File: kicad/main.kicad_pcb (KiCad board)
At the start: 2 copper layers, 200 x 100 mm, 50 parts, among them J1 Barrel_Jack, J2 UART, P1 Mini-DIN_6pins_ver3, SW1 Reset, SW2 SW_Push_DPDT, U1 KM1810VM88, U10 L7805, U11 15 MHz, U12 8255, U13 uSD adapter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

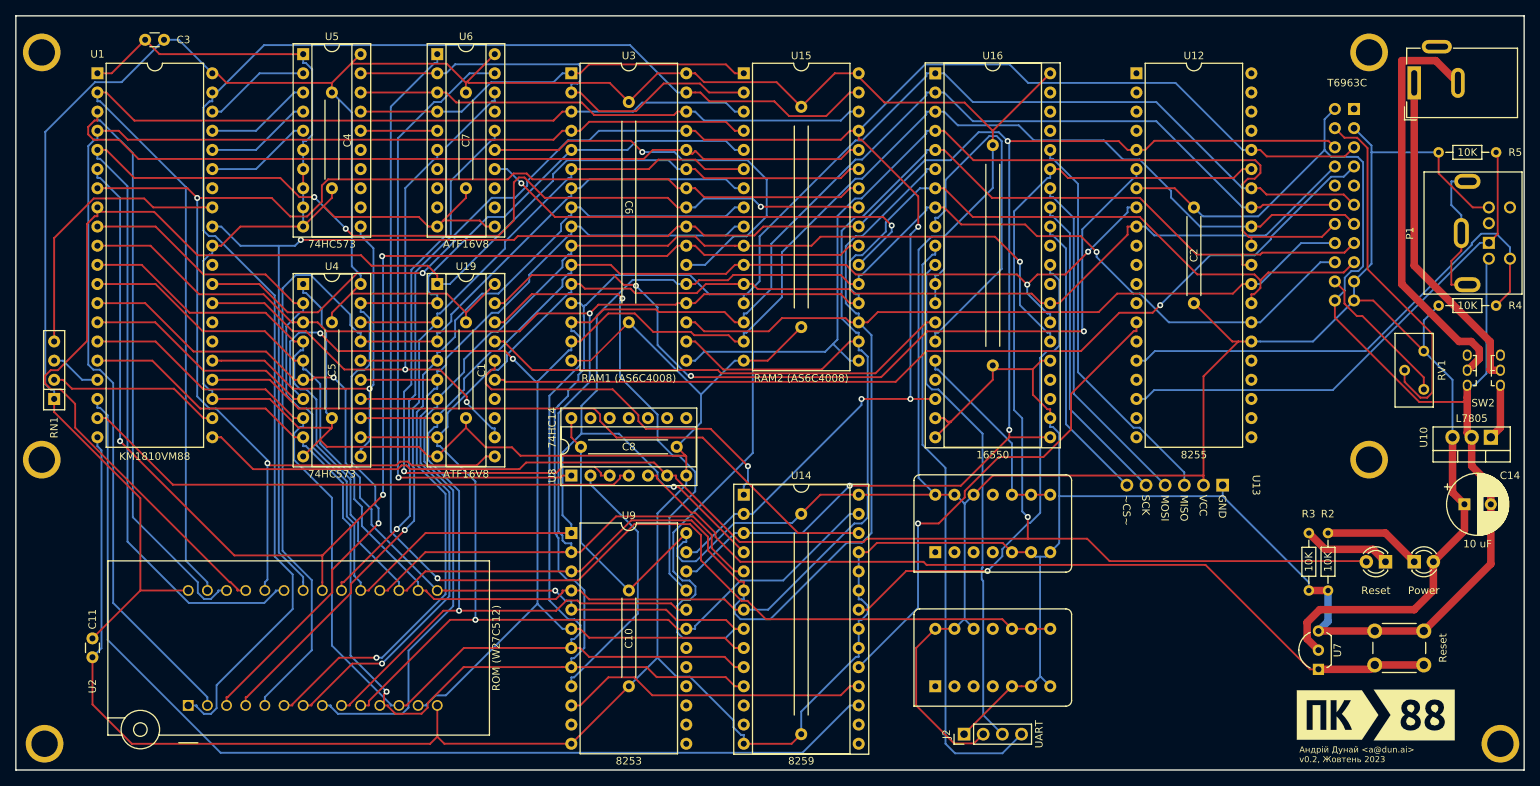
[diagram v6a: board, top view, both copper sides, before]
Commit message: New PCB (add MCB line)
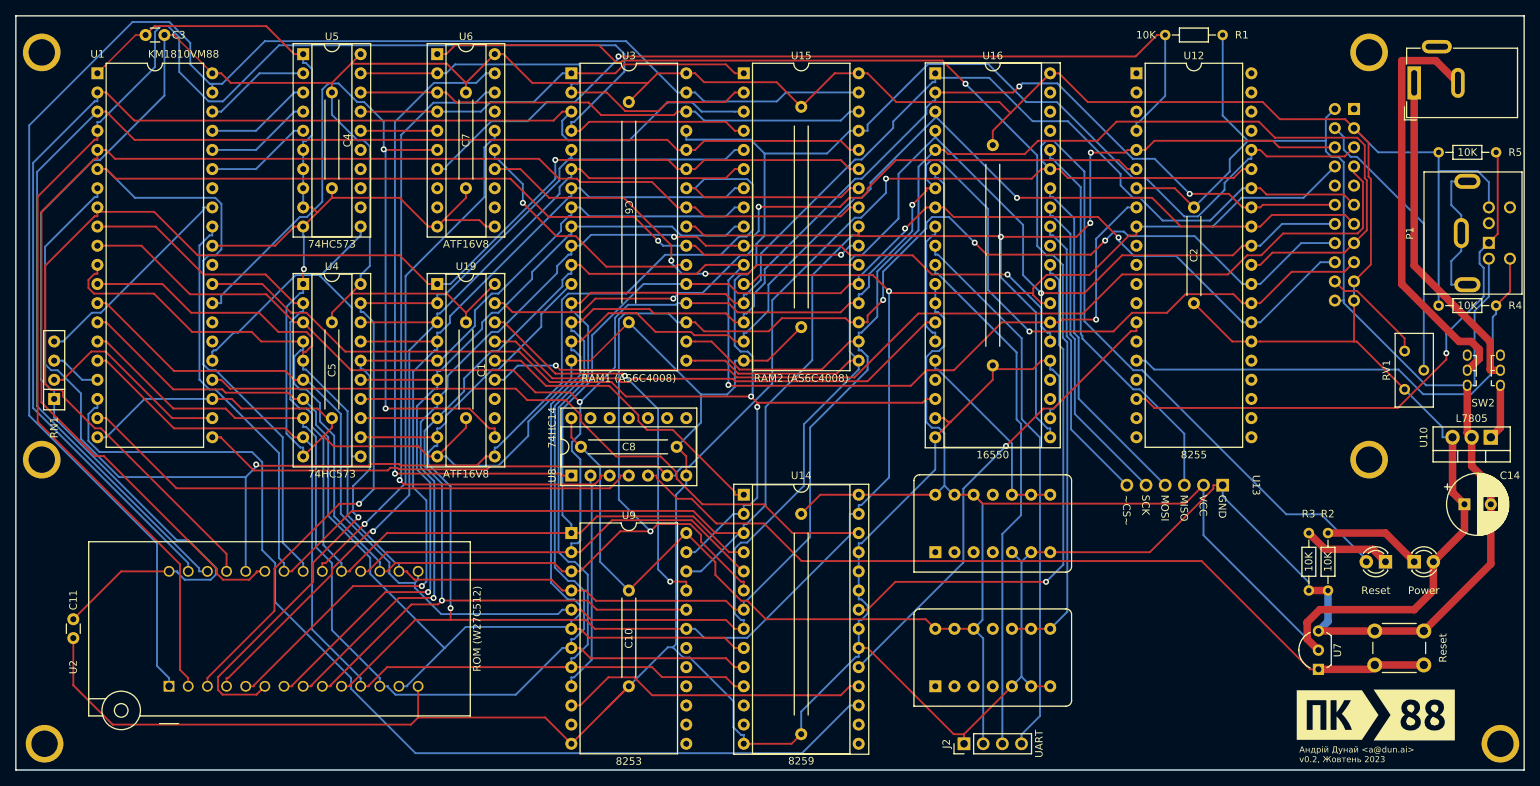
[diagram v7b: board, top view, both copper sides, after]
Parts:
- added R1: 10K, Resistor_THT:R_Axial_DIN0204_L3.6mm_D1.6mm_P7.62mm_Horizontal, F.Cu at (180.3, 20.3)
- moved RV1 5.68 mm to (204.5, 62.2), turned to 90 degrees
- moved C11 3.59 mm to (27.9, 97.8)
- moved U2 3.59 mm to (40.6, 106.7)
- moved J2 1.27 mm to (146.1, 114.3)
- moved C3 0.64 mm to (40.0, 20.3)
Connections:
- U12 pad 4: unconnected-(U12-PA0-Pad4) -> MCB
- U6 pad 7: unconnected-(U6-I-Pad7) -> MCB
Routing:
- net MCB: track 0.00 -> 118.7 mm, vias 0 -> 1
- net +5V: track 696.8 -> 753.1 mm
- net A_{12}: track 171.6 -> 212.0 mm
- net IO/~{M}: track 77.1 -> 108.2 mm
- net Net-(U16-RCLK): track 47.5 -> 16.7 mm
- net LORAM~{EN}: track 56.9 -> 34.0 mm
- net A_{1}: track 206.7 -> 228.8 mm
- net AD_{4}: track 282.7 -> 304.7 mm
- net AD_{5}: track 301.4 -> 279.8 mm, vias 0 -> 4
- net A_{15}: track 190.3 -> 210.1 mm
- net ~{WR}: track 255.3 -> 274.3 mm, vias 4 -> 2
- net PPI~{EN}: track 115.5 -> 97.5 mm, vias 3 -> 2
- net A_{0}: track 255.7 -> 268.7 mm, vias 1 -> 2
- net AD_{6}: track 286.8 -> 299.6 mm, vias 1 -> 3
- net A_{5}: track 137.8 -> 126.0 mm, vias 0 -> 1
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
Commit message: V0.3 WIP
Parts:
- added BZ1: Buzzer, Buzzer_Beeper:Buzzer_TDK_PS1240P02BT_D12.2mm_H6.5mm, F.Cu at (252.1, 47.4)
- added R6: 10K, Resistor_THT:R_Axial_DIN0204_L3.6mm_D1.6mm_P7.62mm_Horizontal, F.Cu at (248.9, 55.9)
- added U20: ATF22V10, Package_DIP:DIP-24_W7.62mm_Socket, F.Cu at (237.8, 42.7)
- moved R4 22.0 mm to (217.5, 35.9), turned to 180 degrees
- moved R5 22.0 mm to (217.5, 56.2), turned to 180 degrees
- moved P1 6.06 mm to (210.8, 44.2), turned to 90 degrees
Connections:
- U12 pad 11: unconnected-(U12-PC6-Pad11) -> Net-(U12-PC6)
- U12 pad 12: unconnected-(U12-PC5-Pad12) -> Net-(U12-PC5)
- U12 pad 13: unconnected-(U12-PC4-Pad13) -> Net-(U12-PC4)
- U12 pad 14: INT1 -> Net-(U12-PC0)
- U12 pad 16: PS2CLK -> unconnected-(U12-PC2-Pad16)
- U12 pad 18: PS2DATA -> T2GATE
- U12 pad 19: unconnected-(U12-PB1-Pad19) -> SPKREN
- U12 pad 22: unconnected-(U12-PB4-Pad22) -> MCB
- U12 pad 4: MCB -> unconnected-(U12-PA0-Pad4)
- U13 pad 3: Net-(U13-MISO) -> Net-(U12-PC0)
- U13 pad 4: Net-(U13-MOSI) -> Net-(U12-PC4)
- U13 pad 5: Net-(U13-SCK) -> Net-(U12-PC5)
- U13 pad 6: Net-(U13-~{CS}) -> Net-(U12-PC6)
- U16 pad 32: Net-(U13-~{CS}) -> unconnected-(U16-~{RTS}-Pad32)
- U16 pad 33: Net-(U13-SCK) -> unconnected-(U16-~{DTR}-Pad33)
- U16 pad 34: Net-(U13-MOSI) -> unconnected-(U16-~{OUT1}-Pad34)
- U16 pad 36: Net-(U13-MISO) -> unconnected-(U16-~{CTS}-Pad36)
- U19 pad 14: unconnected-(U19-I/O-Pad14) -> PS2~{EN}
- U6 pad 12: unconnected-(U6-I/O-Pad12) -> SPKROUT
- U6 pad 8: unconnected-(U6-I-Pad8) -> T2OUT
- U6 pad 9: unconnected-(U6-I-Pad9) -> SPKREN
- U9 pad 16: unconnected-(U9-G2-Pad16) -> T2GATE
- U9 pad 17: unconnected-(U9-OUT2-Pad17) -> T2OUT
- U9 pad 18: unconnected-(U9-CLK2-Pad18) -> TIMERCLK
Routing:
- net GND: track 792.5 -> 0.00 mm, vias 1 -> 0
- net +5V: track 753.1 -> 0.00 mm
- net AD_{0}: track 307.8 -> 0.00 mm
- net AD_{4}: track 304.7 -> 0.00 mm
- net ~{RD}: track 303.3 -> 0.00 mm, vias 3 -> 0
- net AD_{6}: track 299.6 -> 0.00 mm, vias 3 -> 0
- net AD_{1}: track 299.3 -> 0.00 mm, vias 2 -> 0
- net AD_{2}: track 295.9 -> 0.00 mm, vias 1 -> 0
- net AD_{3}: track 288.1 -> 0.00 mm, vias 1 -> 0
- net AD_{5}: track 279.8 -> 0.00 mm, vias 4 -> 0
- net AD_{7}: track 275.3 -> 0.00 mm, vias 2 -> 0
- net ~{WR}: track 274.3 -> 0.00 mm, vias 2 -> 0
- net A_{0}: track 268.7 -> 0.00 mm, vias 2 -> 0
- net RES: track 248.0 -> 0.00 mm, vias 1 -> 0
- net A_{1}: track 228.8 -> 0.00 mm, vias 3 -> 0
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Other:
- board size 200 x 100 mm -> 238.8 x 119.4 mm
